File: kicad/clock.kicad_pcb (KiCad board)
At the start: 2 copper layers, 139.7 x 88.9 mm, 0 parts

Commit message: Some grouping
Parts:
- added C1: 33p, Capacitors_THT:C_Rect_L4.0mm_W2.5mm_P2.50mm, F.Cu at (46.7, 33.9)
- added C2: 33p, Capacitors_THT:C_Rect_L4.0mm_W2.5mm_P2.50mm, F.Cu at (46.7, 27.1)
- added C3: 0u1, Capacitors_THT:CP_Radial_D5.0mm_P2.00mm, F.Cu at (110.5, 142.6)
- added C4: 1u, Capacitors_THT:CP_Radial_D5.0mm_P2.00mm, F.Cu at (127.2, 121.9)
- added C5: 0u1, Capacitors_THT:CP_Radial_D5.0mm_P2.00mm, F.Cu at (123.9, 130.8)
- added D1: D_Schottky_ALT, Diodes_THT:D_A-405_P7.62mm_Horizontal, F.Cu at (85.2, 144.1)
- added Q1: PN2222A, TO_SOT_Packages_THT:TO-92_Molded_Narrow, F.Cu at (175.0, 36.3)
- added Q2: PN2222A, TO_SOT_Packages_THT:TO-92_Molded_Narrow, F.Cu at (177.5, 40.4)
- added Q3: PN2222A, TO_SOT_Packages_THT:TO-92_Molded_Narrow, F.Cu at (65.3, 46.0)
- added Q4: PN2222A, TO_SOT_Packages_THT:TO-92_Molded_Narrow, F.Cu at (62.7, 41.9)
- added Q5: PN2222A, TO_SOT_Packages_THT:TO-92_Molded_Narrow, F.Cu at (210.6, 52.3)
- added Q6: PN2222A, TO_SOT_Packages_THT:TO-92_Molded_Narrow, F.Cu at (213.1, 56.4)
- added R1: 1M, Resistors_THT:R_Axial_DIN0207_L6.3mm_D2.5mm_P10.16mm_Horizontal, F.Cu at (23.5, 25.3)
- added R10: 2k2, Resistors_THT:R_Axial_DIN0207_L6.3mm_D2.5mm_P10.16mm_Horizontal, F.Cu at (172.5, 40.4)
- added R11: 4k7, Resistors_THT:R_Axial_DIN0207_L6.3mm_D2.5mm_P10.16mm_Horizontal, F.Cu at (180.6, 43.4)
- added R12: 470R, Resistors_THT:R_Axial_DIN0207_L6.3mm_D2.5mm_P10.16mm_Horizontal, F.Cu at (207.0, 130.3)
- added R13: 470R, Resistors_THT:R_Axial_DIN0207_L6.3mm_D2.5mm_P10.16mm_Horizontal, F.Cu at (198.4, 130.2)
- added R14: 2k2, Resistors_THT:R_Axial_DIN0207_L6.3mm_D2.5mm_P10.16mm_Horizontal, F.Cu at (67.8, 46.0)
- added R15: 2k2, Resistors_THT:R_Axial_DIN0207_L6.3mm_D2.5mm_P10.16mm_Horizontal, F.Cu at (67.8, 41.9)
- added R16: 2k2, Resistors_THT:R_Axial_DIN0207_L6.3mm_D2.5mm_P10.16mm_Horizontal, F.Cu at (208.0, 52.3)
- added R17: 2k2, Resistors_THT:R_Axial_DIN0207_L6.3mm_D2.5mm_P10.16mm_Horizontal, F.Cu at (208.0, 56.4)
- added R18: 4k7, Resistors_THT:R_Axial_DIN0207_L6.3mm_D2.5mm_P10.16mm_Horizontal, F.Cu at (59.7, 38.9)
- added R19: 4k7, Resistors_THT:R_Axial_DIN0207_L6.3mm_D2.5mm_P10.16mm_Horizontal, F.Cu at (216.2, 59.4)
- added R2: 1M, Resistors_THT:R_Axial_DIN0207_L6.3mm_D2.5mm_P10.16mm_Horizontal, F.Cu at (26.8, 25.3)
- added R20: 470R, Resistors_THT:R_Axial_DIN0207_L6.3mm_D2.5mm_P10.16mm_Horizontal, F.Cu at (190.2, 130.7)
- added R21: 22k, Resistors_THT:R_Axial_DIN0207_L6.3mm_D2.5mm_P10.16mm_Horizontal, F.Cu at (85.2, 135.5)
- added R22: 22k, Resistors_THT:R_Axial_DIN0207_L6.3mm_D2.5mm_P10.16mm_Horizontal, F.Cu at (115.2, 113.6)
- added R23: 22k, Resistors_THT:R_Axial_DIN0207_L6.3mm_D2.5mm_P10.16mm_Horizontal, F.Cu at (85.2, 139.7)
- added R24: 22k, Resistors_THT:R_Axial_DIN0207_L6.3mm_D2.5mm_P10.16mm_Horizontal, F.Cu at (98.5, 131.2)
- added R25: 22k, Resistors_THT:R_Axial_DIN0207_L6.3mm_D2.5mm_P10.16mm_Horizontal, F.Cu at (80.2, 127.0)
- added R26: 22k, Resistors_THT:R_Axial_DIN0207_L6.3mm_D2.5mm_P10.16mm_Horizontal, F.Cu at (93.5, 127.0)
- added R27: 22k, Resistors_THT:R_Axial_DIN0207_L6.3mm_D2.5mm_P10.16mm_Horizontal, F.Cu at (71.8, 144.8)
- added R28: 22k, Resistors_THT:R_Axial_DIN0207_L6.3mm_D2.5mm_P10.16mm_Horizontal, F.Cu at (71.8, 140.6)
- added R29: 22k, Resistors_THT:R_Axial_DIN0207_L6.3mm_D2.5mm_P10.16mm_Horizontal, F.Cu at (71.8, 136.3)
- added R3: 1M, Resistors_THT:R_Axial_DIN0207_L6.3mm_D2.5mm_P10.16mm_Horizontal, F.Cu at (30.1, 25.3)
- added R30: 22k, Resistors_THT:R_Axial_DIN0207_L6.3mm_D2.5mm_P10.16mm_Horizontal, F.Cu at (85.2, 131.2)
- added R31: 2k2, Resistors_THT:R_Axial_DIN0207_L6.3mm_D2.5mm_P10.16mm_Horizontal, F.Cu at (101.8, 113.6)
- added R32: 22k, Resistors_THT:R_Axial_DIN0207_L6.3mm_D2.5mm_P10.16mm_Horizontal, F.Cu at (101.8, 109.3)
- added R33: 22k, Resistors_THT:R_Axial_DIN0207_L6.3mm_D2.5mm_P10.16mm_Horizontal, F.Cu at (101.8, 105.1)
- added R34: 22k, Resistors_THT:R_Axial_DIN0207_L6.3mm_D2.5mm_P10.16mm_Horizontal, F.Cu at (71.8, 132.1)
- added R35: 22k, Resistors_THT:R_Axial_DIN0207_L6.3mm_D2.5mm_P10.16mm_Horizontal, F.Cu at (58.5, 144.8)
- added R36: 22k, Resistors_THT:R_Axial_DIN0207_L6.3mm_D2.5mm_P10.16mm_Horizontal, F.Cu at (58.5, 132.1)
- added R37: 22k, Resistors_THT:R_Axial_DIN0207_L6.3mm_D2.5mm_P10.16mm_Horizontal, F.Cu at (58.5, 140.6)
- added R38: 22k, Resistors_THT:R_Axial_DIN0207_L6.3mm_D2.5mm_P10.16mm_Horizontal, F.Cu at (58.5, 136.3)
- added R39: 22k, Resistors_THT:R_Axial_DIN0207_L6.3mm_D2.5mm_P10.16mm_Horizontal, F.Cu at (101.8, 117.8)
- added R4: 1M, Resistors_THT:R_Axial_DIN0207_L6.3mm_D2.5mm_P10.16mm_Horizontal, F.Cu at (33.4, 25.3)
- added R40: 47R, Resistors_THT:R_Axial_DIN0207_L6.3mm_D2.5mm_P10.16mm_Horizontal, F.Cu at (115.2, 105.1)
- added R41: 2k2, Resistors_THT:R_Axial_DIN0207_L6.3mm_D2.5mm_P10.16mm_Horizontal, F.Cu at (115.2, 109.3)
- added R42: 47R, Resistors_THT:R_Axial_DIN0207_L6.3mm_D2.5mm_P10.16mm_Horizontal, F.Cu at (101.8, 122.1)
- added R5: 1M, Resistors_THT:R_Axial_DIN0207_L6.3mm_D2.5mm_P10.16mm_Horizontal, F.Cu at (36.7, 25.3)
- added R6: 1M, Resistors_THT:R_Axial_DIN0207_L6.3mm_D2.5mm_P10.16mm_Horizontal, F.Cu at (40.0, 25.3)
- added R7: 100k, Resistors_THT:R_Axial_DIN0207_L6.3mm_D2.5mm_P10.16mm_Horizontal, F.Cu at (43.3, 25.3)
- added R8: 470R, Resistors_THT:R_Axial_DIN0207_L6.3mm_D2.5mm_P10.16mm_Horizontal, F.Cu at (214.2, 130.2)
- added R9: 2k2, Resistors_THT:R_Axial_DIN0207_L6.3mm_D2.5mm_P10.16mm_Horizontal, F.Cu at (172.5, 36.3)
- added SW1: SW_DIP_x08, Housings_DIP:DIP-16_W7.62mm, F.Cu at (107.7, 188.6)
- added SW2: SW_Push, Buttons_Switches_THT:SW_TH_Tactile_Omron_B3F-10xx, F.Cu at (128.6, 104.6)
- added SW3: SW_Push, Buttons_Switches_THT:SW_TH_Tactile_Omron_B3F-10xx, F.Cu at (128.6, 112.4)
- added SW4: SW_DIP_x08, Housings_DIP:DIP-16_W7.62mm, F.Cu at (86.5, 188.6)
- added U1: 74HC04, Housings_DIP:DIP-14_W7.62mm, F.Cu at (259.3, 28.1)
- added U10: 7SEGMENT_CC, Displays_7-Segment:HDSP-78xx, F.Cu at (206.2, 121.7)
- added U11: 4543, Housings_DIP:DIP-16_W7.62mm, F.Cu at (193.4, 93.7)
- added U12: 7SEGMENT_CC, Displays_7-Segment:HDSP-78xx, F.Cu at (198.2, 121.7)
- added U13: 4543, Housings_DIP:DIP-16_W7.62mm, F.Cu at (183.4, 93.7)
- added U14: 7SEGMENT_CC, Displays_7-Segment:HDSP-78xx, F.Cu at (190.2, 121.7)
- added U15: 4027, Housings_DIP:DIP-16_W7.62mm, F.Cu at (80.2, 105.0)
- added U16: 74LS390, Housings_DIP:DIP-16_W7.62mm, F.Cu at (91.0, 105.0)
- added U17: 74HC688, Housings_DIP:DIP-20_W7.62mm, F.Cu at (35.4, 70.4)
- added U18: NE555, Housings_DIP:DIP-8_W7.62mm, F.Cu at (111.9, 129.5)
- added U19: 74HC688, Housings_DIP:DIP-20_W7.62mm, F.Cu at (45.5, 70.4)
- added U2: 74LS390, Housings_DIP:DIP-16_W7.62mm, F.Cu at (82.2, 17.7)
- added U3: CD4060, Housings_DIP:DIP-16_W7.62mm, F.Cu at (52.1, 17.7)
- added U4: 4543, Housings_DIP:DIP-16_W7.62mm, F.Cu at (213.5, 93.7)
- added U5: 7SEGMENT_CC, Displays_7-Segment:HDSP-78xx, F.Cu at (214.2, 121.7)
- added U6: 4027, Housings_DIP:DIP-16_W7.62mm, F.Cu at (62.1, 17.7)
- added U7: 74LS390, Housings_DIP:DIP-16_W7.62mm, F.Cu at (92.2, 17.7)
- added U8: 74LS390, Housings_DIP:DIP-16_W7.62mm, F.Cu at (72.1, 17.7)
- added U9: 4543, Housings_DIP:DIP-16_W7.62mm, F.Cu at (203.5, 93.7)
- added Y1: 32768, Crystals:Crystal_DS26_d2.0mm_l6.0mm_Vertical, F.Cu at (46.7, 31.4)
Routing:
- net VCC: track 0.00 -> 51.7 mm
- net Net-(C1-Pad1): track 0.00 -> 43.3 mm
- net GND: track 0.00 -> 31.8 mm
- net Net-(R6-Pad2): track 0.00 -> 30.0 mm
- net 1min: track 0.00 -> 26.0 mm
- net 1hr: track 0.00 -> 22.2 mm
- net /Q3: track 0.00 -> 21.0 mm
- net /S3: track 0.00 -> 21.0 mm
- net Net-(R14-Pad2): track 0.00 -> 17.5 mm
- net /Q0: track 0.00 -> 16.8 mm
- net /S0: track 0.00 -> 16.7 mm
- net Net-(U8-Pad15): track 0.00 -> 16.5 mm
- net /R0: track 0.00 -> 14.5 mm
- net /T0: track 0.00 -> 14.2 mm
- net /S1: track 0.00 -> 11.7 mm
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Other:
- board outline removed
- net class Default: via_dia 0.6 -> 0.8
- rule pad_to_mask_clearance: 0.2 -> 0

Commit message: Fixed buses between sheets; comparator BCD inputs connected
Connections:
- R16 pad 2: /S1 -> HL1
- R17 pad 2: (no net) -> HH1
- R9 pad 2: /R1 -> MH1
- U11 pad 2: /S2 -> HL2
- U11 pad 3: /S1 -> HL1
- U11 pad 4: /S3 -> HL3
- U11 pad 5: /S0 -> HL0
- U13 pad 2: /T2 -> HH2
- U13 pad 3: /T1 -> HH1
- U13 pad 4: /T3 -> HH3
- U13 pad 5: /T0 -> HH0
- U17 pad 11: (no net) -> ML3
- U17 pad 13: (no net) -> ML2
- U17 pad 15: (no net) -> ML1
- U17 pad 17: (no net) -> ML0
- U17 pad 2: (no net) -> MH3
- U17 pad 4: (no net) -> 1hr
- U17 pad 6: (no net) -> MH1
- U17 pad 8: (no net) -> MH0
- U19 pad 11: (no net) -> HL3
- U19 pad 13: (no net) -> HL2
- U19 pad 15: (no net) -> HL1
- U19 pad 17: (no net) -> HL0
- U19 pad 2: (no net) -> HH3
- U19 pad 4: (no net) -> HH2
- U19 pad 6: (no net) -> HH1
- U19 pad 8: (no net) -> HH0
- U2 pad 11: /R1 -> MH1
- U2 pad 12: /R0 -> MH0
- U2 pad 13: /R0 -> MH0
- U2 pad 15: /Q3 -> ML3
- U2 pad 3: /Q0 -> ML0
- U2 pad 4: /Q0 -> ML0
- U2 pad 5: /Q1 -> ML1
- U2 pad 6: /Q2 -> ML2
- U2 pad 7: /Q3 -> ML3
- U2 pad 9: /R3 -> MH3
- U4 pad 2: /Q2 -> ML2
- U4 pad 3: /Q1 -> ML1
- U4 pad 4: /Q3 -> ML3
- U4 pad 5: /Q0 -> ML0
- U7 pad 10: /T2 -> HH2
- U7 pad 11: /T1 -> HH1
- U7 pad 12: /T0 -> HH0
- U7 pad 13: /T0 -> HH0
- U7 pad 15: /S3 -> HL3
- U7 pad 3: /S0 -> HL0
- U7 pad 4: /S0 -> HL0
- U7 pad 5: /S1 -> HL1
- U7 pad 6: /S2 -> HL2
- U7 pad 7: /S3 -> HL3
- U7 pad 9: /T3 -> HH3
- U9 pad 3: /R1 -> MH1
- U9 pad 4: /R3 -> MH3
- U9 pad 5: /R0 -> MH0
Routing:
- net ML3: track 0.00 -> 21.0 mm
- net /Q3: track 21.0 -> 0.00 mm
- net HL3: track 0.00 -> 21.0 mm
- net /S3: track 21.0 -> 0.00 mm
- net ML0: track 0.00 -> 16.8 mm
- net /Q0: track 16.8 -> 0.00 mm
- net HL0: track 0.00 -> 16.7 mm
- net /S0: track 16.7 -> 0.00 mm
- net MH0: track 0.00 -> 14.5 mm
- net /R0: track 14.5 -> 0.00 mm
- net HH0: track 0.00 -> 14.2 mm
- net /T0: track 14.2 -> 0.00 mm
- net HL1: track 0.00 -> 11.7 mm
- net /S1: track 11.7 -> 0.00 mm
- net ML1: track 0.00 -> 11.3 mm
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
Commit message: Now how to route the BCD buses?
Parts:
- moved R31 150.5 mm to (249.7, 141.6)
- moved U4 148.0 mm to (69.7, 58.7), turned to 180 degrees
- moved U18 138.7 mm to (250.6, 127.0)
- moved C4 137.8 mm to (264.5, 133.5)
- moved R41 135.6 mm to (250.4, 119.8)
- moved U9 128.6 mm to (79.8, 58.7), turned to 180 degrees
- moved U11 109.4 mm to (89.8, 58.7), turned to 180 degrees
- moved R22 95.2 mm to (20.3, 121.8)
- moved U13 90.6 mm to (99.8, 58.7), turned to 180 degrees
- moved R24 77.9 mm to (20.6, 129.9)
- moved R26 73.7 mm to (20.8, 139.1)
- moved R40 70.3 mm to (143.8, 169.3)
- moved R39 67.2 mm to (42.3, 148.8)
- moved R21 66.8 mm to (20.7, 117.7)
- moved R23 66.2 mm to (20.3, 126.4)
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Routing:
- net Net-(R14-Pad2): track 17.5 -> 0.00 mm
- net ML0: track 16.8 -> 2.54 mm
- net HH0: track 14.2 -> 2.54 mm
- net ML1: track 11.3 -> 0.00 mm
- net 1min: track 26.0 -> 16.2 mm
- net HH1: track 9.14 -> 0.00 mm
- net ML2: track 8.22 -> 0.00 mm
- net GND: track 31.8 -> 25.0 mm
- net HH2: track 6.35 -> 0.00 mm
- net ML3: track 21.0 -> 15.9 mm
- net HH3: track 3.45 -> 0.00 mm

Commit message: One 7-seg display routed
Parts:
- moved R1 197.4 mm to (201.8, 109.9), turned to 90 degrees
- moved R2 191.4 mm to (198.5, 109.9), turned to 90 degrees
- moved R3 185.5 mm to (195.2, 109.9), turned to 90 degrees
- moved R18 182.6 mm to (201.5, 88.3), turned to 90 degrees
- moved R4 179.7 mm to (191.9, 109.9), turned to 90 degrees
- moved Q4 175.3 mm to (198.5, 85.2), turned to 180 degrees
- moved R5 173.9 mm to (188.6, 109.9), turned to 90 degrees
- moved Q3 168.8 mm to (196.0, 81.2), turned to 0 degrees
- moved R6 168.1 mm to (185.3, 109.9), turned to 90 degrees
- moved R15 165.4 mm to (193.4, 85.2), turned to 180 degrees
- moved R14 163.8 mm to (193.4, 81.2), turned to 180 degrees
- moved R7 162.4 mm to (182.0, 109.9), turned to 90 degrees
- moved U3 157.0 mm to (173.2, 117.5), turned to 180 degrees
- moved C2 154.7 mm to (178.6, 108.1), turned to 180 degrees
- moved U16 153.4 mm to (234.9, 24.6)
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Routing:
- net Net-(U13-Pad9): track 0.00 -> 29.1 mm, vias 0 -> 1
- net Net-(U13-Pad13): track 0.00 -> 24.3 mm
- net Net-(U13-Pad10): track 0.00 -> 24.1 mm, vias 0 -> 1
- net Net-(U13-Pad12): track 0.00 -> 23.6 mm
- net Net-(U13-Pad14): track 0.00 -> 21.7 mm, vias 0 -> 1
- net Net-(U13-Pad11): track 0.00 -> 21.1 mm
- net Net-(U13-Pad15): track 0.00 -> 16.4 mm, vias 0 -> 1
- net Net-(R20-Pad1): track 0.00 -> 5.08 mm

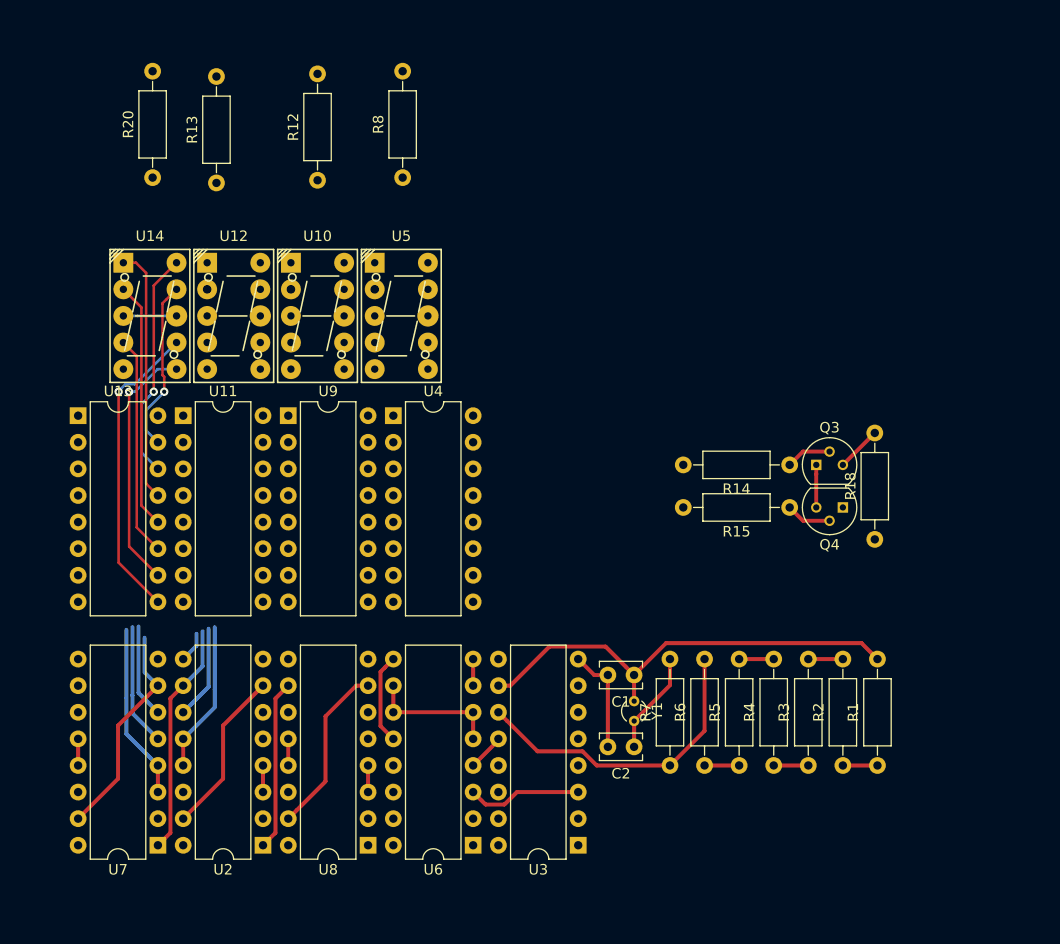
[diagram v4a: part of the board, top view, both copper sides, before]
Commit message: BCD output bus available
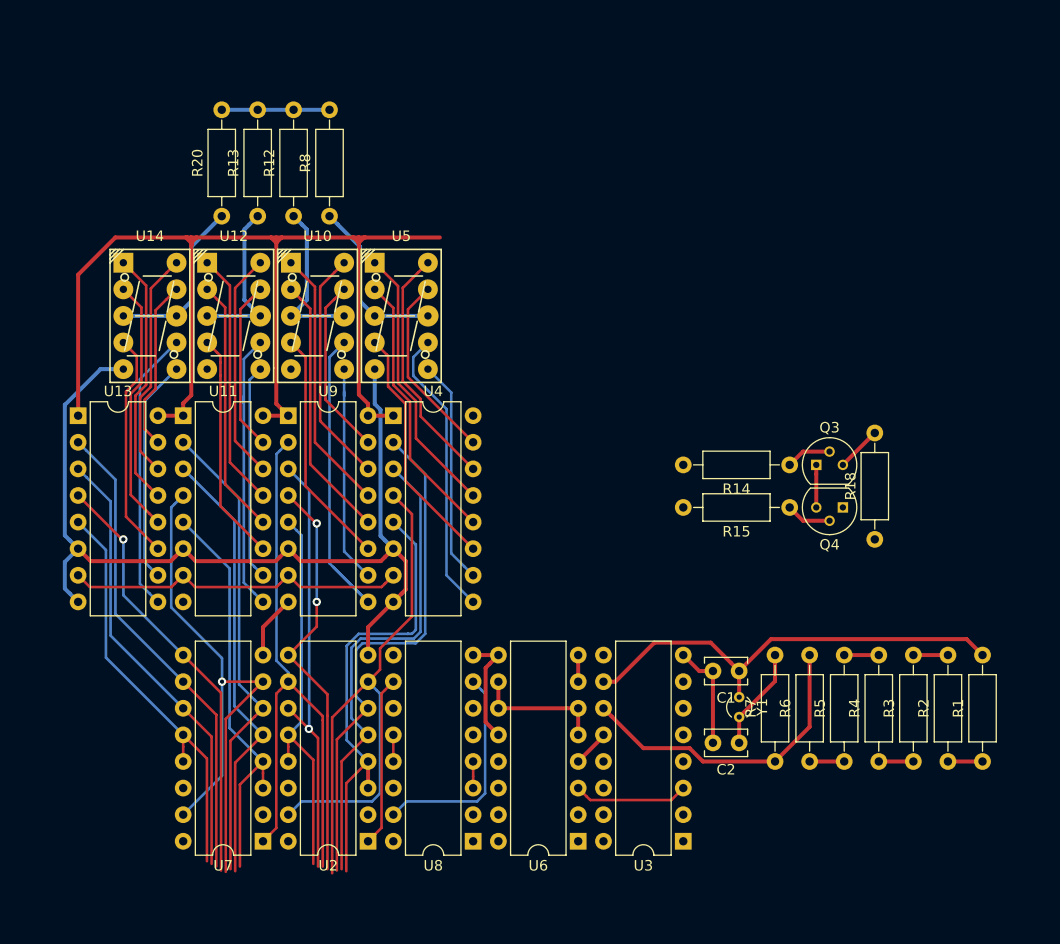
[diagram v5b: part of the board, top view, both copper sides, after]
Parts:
- moved R1 10.0 mm to (211.8, 109.5)
- moved R4 10.0 mm to (201.9, 109.5)
- moved U2 10.0 mm to (153.2, 117.1)
- moved U6 10.0 mm to (173.2, 117.1)
- moved Y1 10.0 mm to (188.6, 103.3)
- moved C1 10.0 mm to (188.6, 100.8)
- moved C2 10.0 mm to (188.6, 107.7)
- moved R2 10.0 mm to (208.5, 109.5)
- moved R3 10.0 mm to (205.2, 109.5)
- moved R5 10.0 mm to (198.6, 109.5)
- moved R6 10.0 mm to (195.3, 109.5)
- moved R7 10.0 mm to (192.0, 109.5)
- moved U3 10.0 mm to (183.3, 117.1)
- moved U7 10.0 mm to (143.1, 117.1)
- moved U8 10.0 mm to (163.2, 117.1)
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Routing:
- net VCC: track 51.7 -> 166.1 mm
- net GND: track 25.0 -> 134.3 mm
- net ML2: track 0.00 -> 49.6 mm
- net ML1: track 0.00 -> 46.7 mm
- net HH2: track 0.00 -> 46.0 mm
- net ML3: track 15.9 -> 60.7 mm
- net HH1: track 0.00 -> 43.0 mm
- net ML0: track 2.54 -> 44.2 mm
- net HH3: track 0.00 -> 41.5 mm, vias 0 -> 1
- net HH0: track 2.54 -> 40.0 mm
- net HL3: track 21.0 -> 58.0 mm, vias 0 -> 1
- net 1hr: track 22.2 -> 59.0 mm
- net MH3: track 2.94 -> 39.5 mm, vias 0 -> 2
- net HL2: track 8.95 -> 45.2 mm
- net MH1: track 8.98 -> 42.0 mm, vias 0 -> 1
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
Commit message: More routing, but oops displays are backwards and it's all for nothing
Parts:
- removed the R12 at (146.1, 57.4)
- removed the R13 at (142.6, 57.4)
- removed the R8 at (149.5, 57.4)
- added R18: 1k, Resistors_THT:R_Axial_DIN0207_L6.3mm_D2.5mm_P10.16mm_Horizontal, F.Cu at (165.5, 61.8)
- added TP1: 0.5 Hz, clock:TestPoint, F.Cu at (165.6, 119.8)
- R18: renamed from R20; value 470R -> 1k
- moved U17 101.2 mm to (148.0, 120.4), turned to 0 degrees
- moved U19 98.9 mm to (135.5, 120.4), turned to 0 degrees
- moved R18 23.4 mm to (162.2, 61.8), turned to 270 degrees
- moved U16 9.70 mm to (86.4, 112.5)
- moved SW1 3.05 mm to (104.6, 188.7)
- moved SW4 3.05 mm to (83.4, 188.7)
- renumbered R11 to R10, R14 to R11, R15 to R12, R16 to R13, R17 to R14, R18 to R15, R19 to R16, R21 to R19, R22 to R20, R23 to R21, R24 to R22, R25 to R23, R26 to R24, R27 to R25, R28 to R26, R29 to R27, R30 to R28, R31 to R29, R40 to R30, R32 to R31, R33 to R32, R34 to R33, R35 to R34, R36 to R35, R37 to R36, R38 to R37, R39 to R38, R41 to R39, R42 to R40, R9 to R8, R10 to R9, U16 to U15, U15 to U16
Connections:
- R18 pad 1: Net-(R20-Pad1) -> Net-(R17-Pad1)
- U10 pad 3: Net-(R12-Pad1) -> Net-(R17-Pad1)
- U10 pad 8: Net-(R12-Pad1) -> Net-(R17-Pad1)
- U12 pad 3: Net-(R13-Pad1) -> Net-(R17-Pad1)
- U12 pad 8: Net-(R13-Pad1) -> Net-(R17-Pad1)
- U14 pad 3: Net-(R20-Pad1) -> Net-(R17-Pad1)
- U14 pad 8: Net-(R20-Pad1) -> Net-(R17-Pad1)
- U5 pad 3: Net-(R8-Pad1) -> Net-(R17-Pad1)
- U5 pad 8: Net-(R8-Pad1) -> Net-(R17-Pad1)
- U6 pad 15: (no net) -> 0.5Hz
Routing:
- net VCC: track 166.1 -> 219.6 mm
- net Net-(R17-Pad1): track 0.00 -> 39.7 mm
- net ML3: track 60.7 -> 86.2 mm
- net HL3: track 58.0 -> 82.8 mm
- net HH0: track 40.0 -> 63.0 mm
- net MH0: track 37.2 -> 58.3 mm
- net HL2: track 45.2 -> 65.2 mm
- net ML2: track 49.6 -> 68.4 mm
- net HH1: track 43.0 -> 60.5 mm
- net Net-(R8-Pad1): track 16.4 -> 0.00 mm
- net Net-(R20-Pad1): track 16.4 -> 0.00 mm
- net MH1: track 42.0 -> 57.9 mm
- net Net-(R13-Pad1): track 15.8 -> 0.00 mm
- net Net-(R12-Pad1): track 15.8 -> 0.00 mm
- net HL1: track 42.7 -> 57.2 mm
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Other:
- board outline added: 100 x 100 mm
- board text added: "FIXME: 7-SEGMENT DISPLAYS ARE BACKWARDS!"
